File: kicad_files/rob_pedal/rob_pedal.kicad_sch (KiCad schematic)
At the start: 52 parts, among them J1 OD_IN, J2 ODR_OUT, J3 9V, J4 SHO_IN, J5 SHO_OUT, Q1 BS170, Q2 BS170, Q3 BS170, Q4 BS170

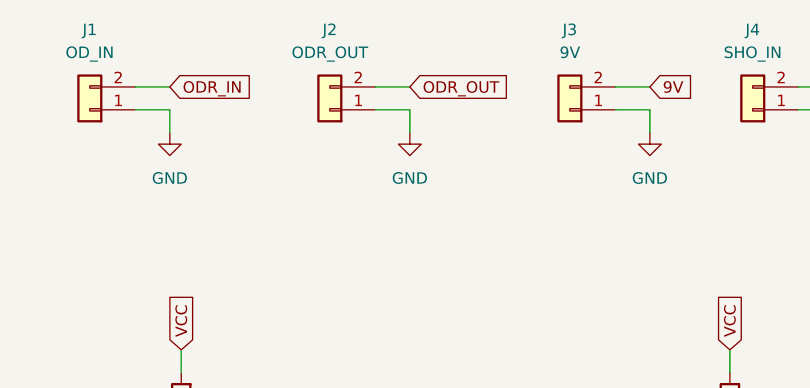
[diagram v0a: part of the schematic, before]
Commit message: added silkscreen and logo
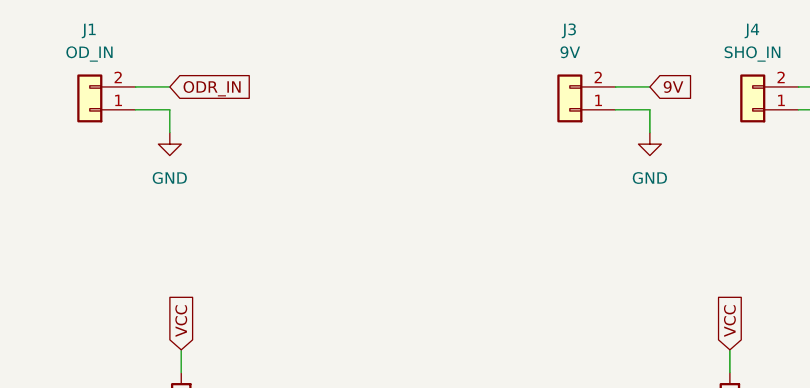
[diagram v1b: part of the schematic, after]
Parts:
- removed J2: ODR_OUT, Connector_Wire:SolderWire-0.5sqmm_1x02_P4.6mm_D0.9mm_OD2.1mm, symbol Connector_Generic:Conn_01x02
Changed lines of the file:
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@@
-    (stroke (width 0) (type default) (color 0 0 0 0))
-  )
-  (wire (pts (xy 87.63 54.61) (xy 87.63 52.07))
     (stroke (width 0) (type default) (color 0 0 0 0))
   )
@@
     (stroke (width 0) (type default) (color 0 0 0 0))
   )
-  (wire (pts (xy 83.82 49.53) (xy 87.63 49.53))
-    (stroke (width 0) (type default) (color 0 0 0 0))
-  )
   (wire (pts (xy 100.33 110.49) (xy 102.87 110.49))
     (stroke (width 0) (type default) (color 0 0 0 0))
@@
   )
   (wire (pts (xy 50.8 104.14) (xy 50.8 109.22))
-    (stroke (width 0) (type default) (color 0 0 0 0))
-  )
-  (wire (pts (xy 83.82 52.07) (xy 87.63 52.07))
     (stroke (width 0) (type default) (color 0 0 0 0))
   )
@@
     )
   )
-  (global_label "ODR_OUT" (shape input) (at 87.63 49.53 0) (fields_autoplaced)
-    (effects (font (size 1.27 1.27)) (justify left))
-    (property "Referenzen zwischen Schaltplänen" "${INTERSHEET_REFS}" (id 0) (at 98.5098 49.4506 0)
-      (effects (font (size 1.27 1.27)) (justify left) hide)
-    )
-  )
   (global_label "ODR_OUT" (shape input) (at 269.24 96.52 0) (fields_autoplaced)
     (effects (font (size 1.27 1.27)) (justify left))
@@
     (pin "1")
   )
-  (symbol (lib_id "power:GND") (at 87.63 54.61 0) (unit 1)
-    (in_bom yes) (on_board yes) (fields_autoplaced)
-    (property "Reference" "#PWR0120" (id 0) (at 87.63 60.96 0)
-      (effects (font (size 1.27 1.27)) hide)
-    )
-    (property "Value" "GND" (id 1) (at 87.63 59.69 0))
-    (property "Footprint" "" (id 2) (at 87.63 54.61 0)
-      (effects (font (size 1.27 1.27)) hide)
-    )
-    (property "Datasheet" "" (id 3) (at 87.63 54.61 0)
-      (effects (font (size 1.27 1.27)) hide)
-    )
-    (pin "1")
-  )
   (symbol (lib_id "Connector_Generic:Conn_01x02") (at 125.73 52.07 180) (unit 1)
     (in_bom yes) (on_board yes) (fields_autoplaced)
@@
     (pin "2")
   )
-  (symbol (lib_id "Connector_Generic:Conn_01x02") (at 78.74 52.07 180) (unit 1)
-    (in_bom yes) (on_board yes) (fields_autoplaced)
-    (property "Reference" "J2" (id 0) (at 78.74 43.18 0))
-    (property "Value" "ODR_OUT" (id 1) (at 78.74 45.72 0))
-    (property "Footprint" "Connector_Wire:SolderWire-0.5sqmm_1x02_P4.6mm_D0.9mm_OD2.1mm" (id 2) (at 78.74 52.07 0)
-      (effects (font (size 1.27 1.27)) hide)
-    )
-    (property "Datasheet" "~" (id 3) (at 78.74 52.07 0)
-      (effects (font (size 1.27 1.27)) hide)
-    )
-    (pin "1")
-    (pin "2")
-  )
   (symbol (lib_id "Device:R_Potentiometer") (at 69.85 129.54 0) (unit 1)
     (in_bom yes) (on_board yes) (fields_autoplaced)
@@
       (reference "#PWR0119") (unit 1) (value "GND") (footprint "")
     )
-    (path "/59962239-5519-43fe-b620-ce1ec62e34cc"
-      (reference "#PWR0120") (unit 1) (value "GND") (footprint "")
-    )
     (path "/4f713451-5a24-4a67-abb7-d76997d28803"
       (reference "#PWR0121") (unit 1) (value "GND") (footprint "")
@@
       (reference "J1") (unit 1) (value "OD_IN") (footprint "Connector_Wire:SolderWire-0.5sqmm_1x02_P4.6mm_D0.9mm_OD2.1mm")
     )
-    (path "/ce489faf-45da-44c4-8c7e-abb7ca7b8c49"
-      (reference "J2") (unit 1) (value "ODR_OUT") (footprint "Connector_Wire:SolderWire-0.5sqmm_1x02_P4.6mm_D0.9mm_OD2.1mm")
-    )
     (path "/7d22d38f-2ccf-4d2a-a916-263ee3005e43"
